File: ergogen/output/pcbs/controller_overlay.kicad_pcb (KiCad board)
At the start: 2 copper layers, 20 x 60.6 mm, 0 parts

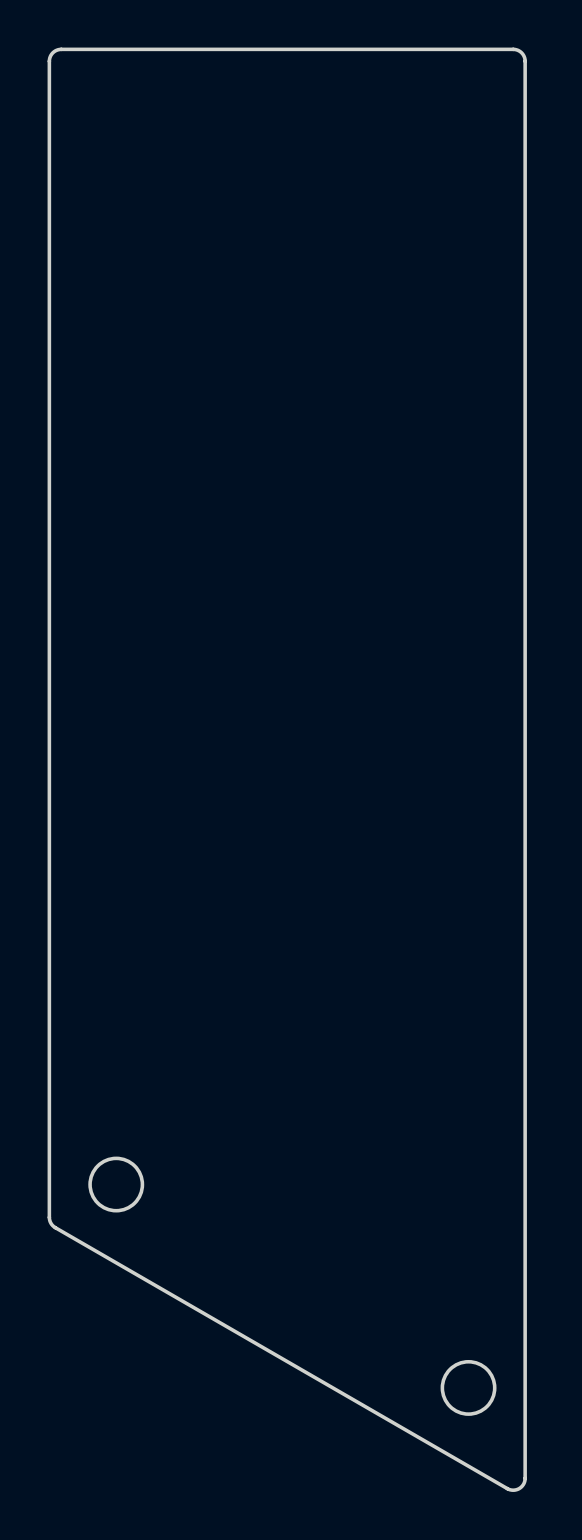
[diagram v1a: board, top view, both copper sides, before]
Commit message: Fix key positions to exactly match the corne
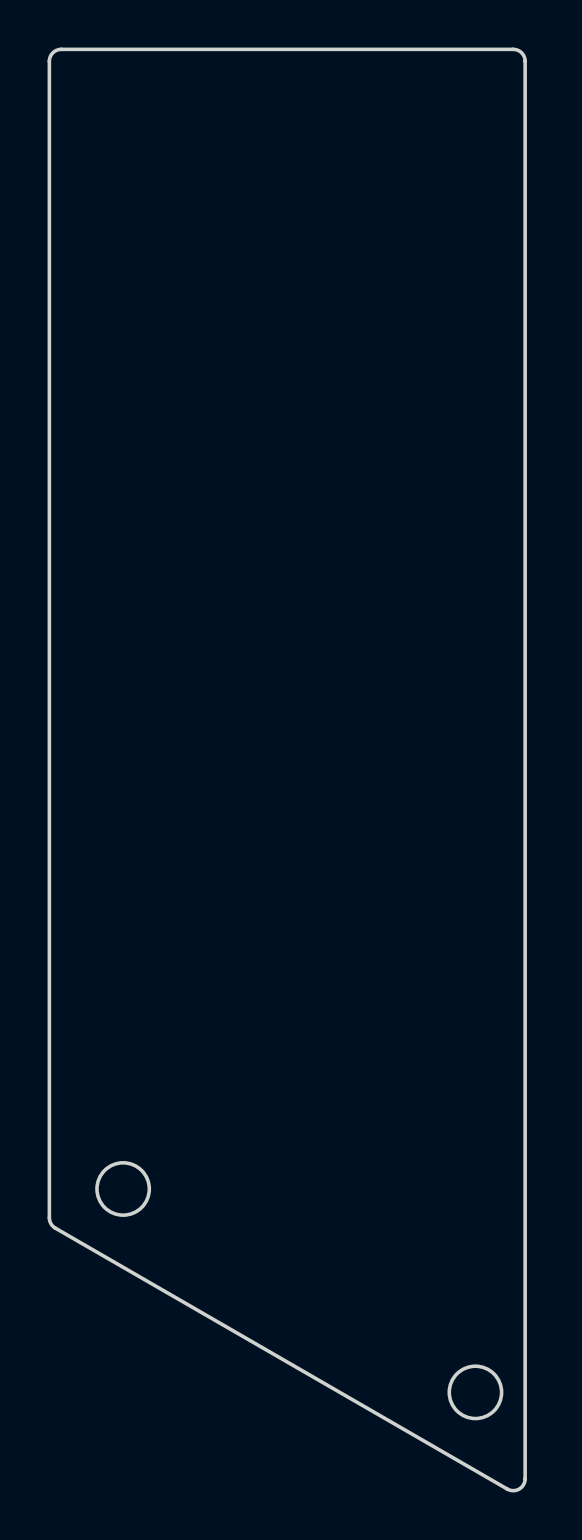
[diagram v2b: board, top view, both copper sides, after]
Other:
- outline, holes or cut-outs redrawn
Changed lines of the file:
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@@
     (add_net "")
   )
-            (gr_line (start 224.5 112.5673240447331) (end 224.5 53) (angle 90) (layer Edge.Cuts) (width 0.15))
+            (gr_line (start 224.5 112.58641018336651) (end 224.5 53) (angle 90) (layer Edge.Cuts) (width 0.15))
 (gr_line (start 224 52.5) (end 205 52.5) (angle 90) (layer Edge.Cuts) (width 0.15))
-(gr_line (start 204.5 53) (end 204.5 101.59766890124159) (angle 90) (layer Edge.Cuts) (width 0.15))
-(gr_line (start 223.74999999999997 113.00033674473308) (end 204.75 102.0306816012416) (angle 90) (layer Edge.Cuts) (width 0.15))
+(gr_line (start 204.5 53) (end 204.5 101.616755039875) (angle 90) (layer Edge.Cuts) (width 0.15))
+(gr_line (start 223.74999999999997 113.01942288336649) (end 204.75 102.04976773987501) (angle 90) (layer Edge.Cuts) (width 0.15))
 (gr_arc (start 224 53) (end 224.5 53) (angle -90) (layer Edge.Cuts) (width 0.15))
 (gr_arc (start 205 53) (end 205 52.5) (angle -90) (layer Edge.Cuts) (width 0.15))
-(gr_arc (start 205 101.59766890124159) (end 204.5 101.59766890124159) (angle -59.999999891584196) (layer Edge.Cuts) (width 0.15))
-(gr_arc (start 224 112.5673240447331) (end 223.75 113.0003367447331) (angle -120.0000001084203) (layer Edge.Cuts) (width 0.15))
-(gr_circle (center 207.31164829999997 100.2187534) (end 208.41164829999997 100.2187534) (layer Edge.Cuts) (width 0.15))
-(gr_circle (center 222.12068269999997 108.7687534) (end 223.22068269999997 108.7687534) (layer Edge.Cuts) (width 0.15))
+(gr_arc (start 205 101.616755039875) (end 204.5 101.616755039875) (angle -59.999999891584196) (layer Edge.Cuts) (width 0.15))
+(gr_arc (start 224 112.58641018336651) (end 223.75 113.01942288336652) (angle -120.0000001084203) (layer Edge.Cuts) (width 0.15))
+(gr_circle (center 207.6013921 100.4051232) (end 208.7013921 100.4051232) (layer Edge.Cuts) (width 0.15))
+(gr_circle (center 222.4104265 108.9551232) (end 223.5104265 108.9551232) (layer Edge.Cuts) (width 0.15))
 )

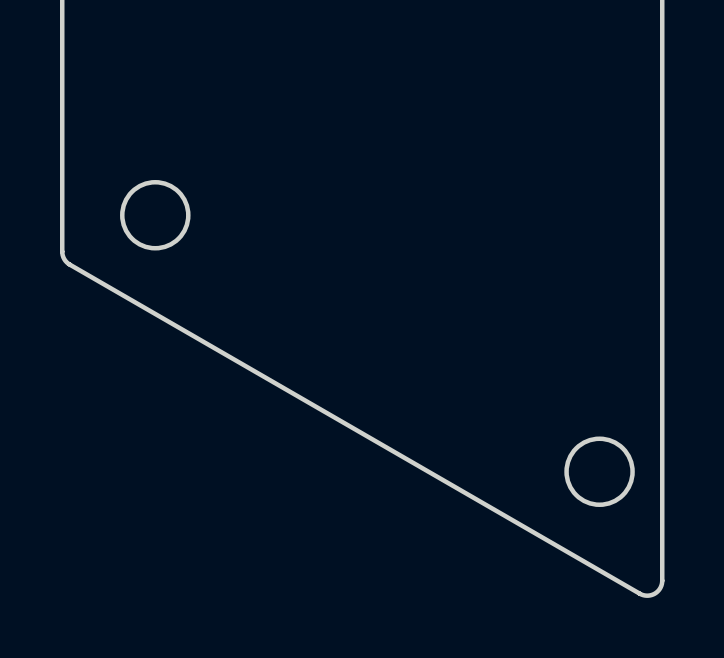
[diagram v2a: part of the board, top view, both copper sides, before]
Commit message: Fix MCU cover mounting holes position
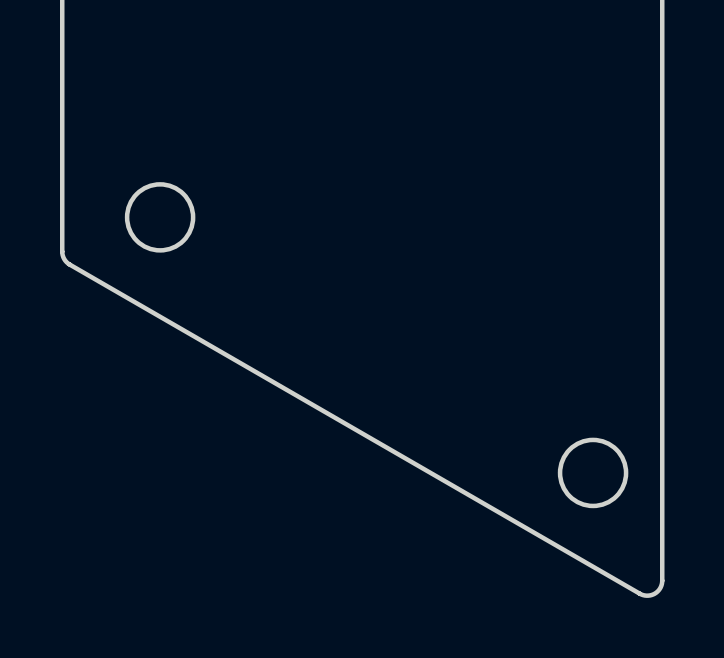
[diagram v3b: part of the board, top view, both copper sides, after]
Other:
- outline, holes or cut-outs redrawn
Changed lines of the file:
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@@
 (gr_arc (start 205 101.616755039875) (end 204.5 101.616755039875) (angle -59.999999891584196) (layer Edge.Cuts) (width 0.15))
 (gr_arc (start 224 112.58641018336651) (end 223.75 113.01942288336652) (angle -120.0000001084203) (layer Edge.Cuts) (width 0.15))
-(gr_circle (center 207.6013921 100.4051232) (end 208.7013921 100.4051232) (layer Edge.Cuts) (width 0.15))
-(gr_circle (center 222.4104265 108.9551232) (end 223.5104265 108.9551232) (layer Edge.Cuts) (width 0.15))
+(gr_circle (center 207.762 100.476) (end 208.862 100.476) (layer Edge.Cuts) (width 0.15))
+(gr_circle (center 222.194 108.995) (end 223.29399999999998 108.995) (layer Edge.Cuts) (width 0.15))
 )

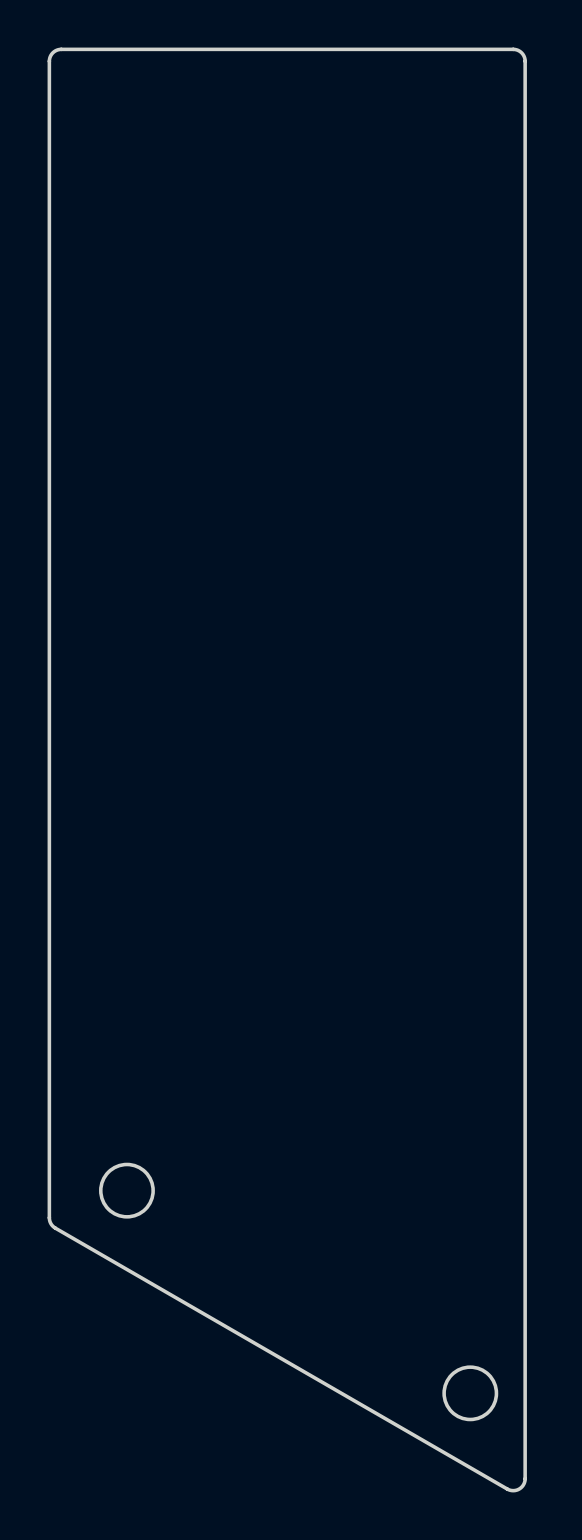
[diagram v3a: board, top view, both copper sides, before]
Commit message: Overhaul outlines making use of intersect
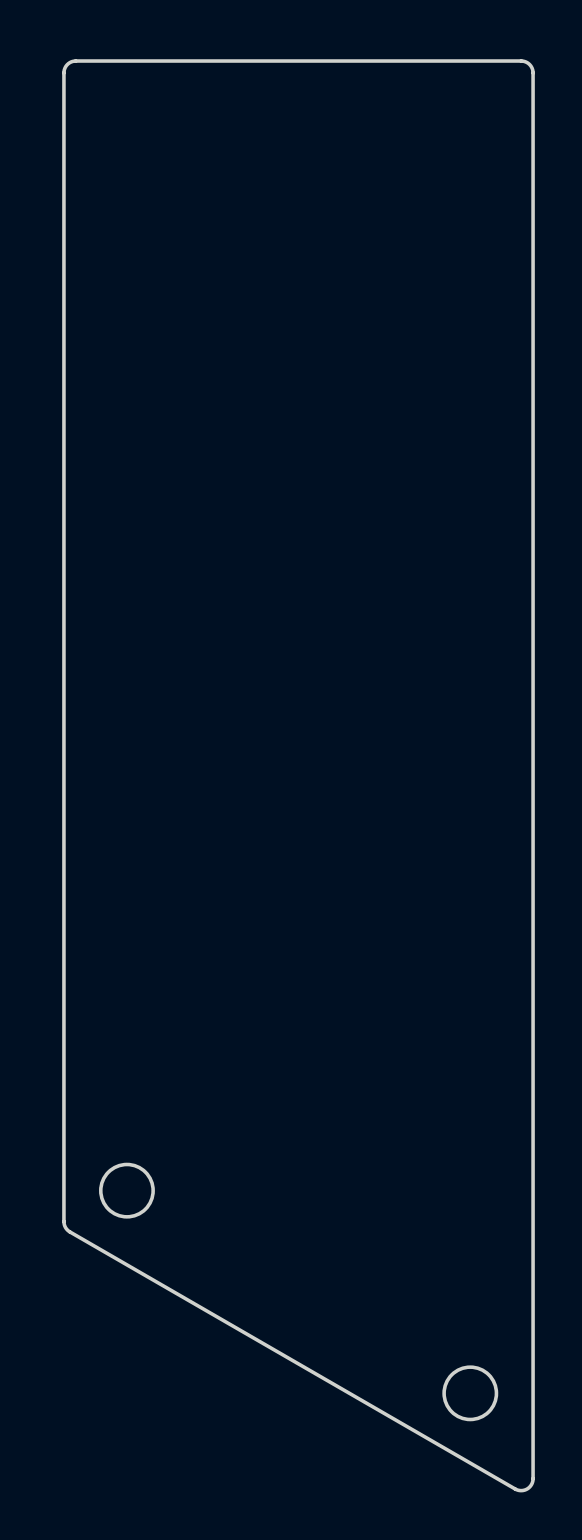
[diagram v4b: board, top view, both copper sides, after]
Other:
- board size 20 x 60.6 mm -> 19.7 x 60.1 mm
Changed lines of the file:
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@@
     (add_net "")
   )
-            (gr_line (start 224.5 112.58641018336651) (end 224.5 53) (angle 90) (layer Edge.Cuts) (width 0.15))
-(gr_line (start 224 52.5) (end 205 52.5) (angle 90) (layer Edge.Cuts) (width 0.15))
-(gr_line (start 204.5 53) (end 204.5 101.616755039875) (angle 90) (layer Edge.Cuts) (width 0.15))
-(gr_line (start 223.74999999999997 113.01942288336649) (end 204.75 102.04976773987501) (angle 90) (layer Edge.Cuts) (width 0.15))
-(gr_arc (start 224 53) (end 224.5 53) (angle -90) (layer Edge.Cuts) (width 0.15))
-(gr_arc (start 205 53) (end 205 52.5) (angle -90) (layer Edge.Cuts) (width 0.15))
-(gr_arc (start 205 101.616755039875) (end 204.5 101.616755039875) (angle -59.999999891584196) (layer Edge.Cuts) (width 0.15))
-(gr_arc (start 224 112.58641018336651) (end 223.75 113.01942288336652) (angle -120.0000001084203) (layer Edge.Cuts) (width 0.15))
+            (gr_line (start 205.113 101.77697755907997) (end 205.113 53.49) (angle 90) (layer Edge.Cuts) (width 0.15))
+(gr_line (start 205.613 52.99) (end 224.333 52.99) (angle 90) (layer Edge.Cuts) (width 0.15))
+(gr_line (start 224.833 53.49) (end 224.833 112.58497459811554) (angle 90) (layer Edge.Cuts) (width 0.15))
+(gr_line (start 224.08299999999997 113.01798729811554) (end 205.36299999999997 102.20999025907994) (angle 90) (layer Edge.Cuts) (width 0.15))
+(gr_arc (start 205.613 53.49) (end 205.613 52.99) (angle -90) (layer Edge.Cuts) (width 0.15))
+(gr_arc (start 224.333 53.49) (end 224.833 53.49) (angle -90) (layer Edge.Cuts) (width 0.15))
+(gr_arc (start 224.333 112.58497459811554) (end 224.083 113.01798729811554) (angle -120.00000010841867) (layer Edge.Cuts) (width 0.15))
+(gr_arc (start 205.613 101.77697755907997) (end 205.113 101.77697755907997) (angle -59.999999891579705) (layer Edge.Cuts) (width 0.15))
 (gr_circle (center 207.762 100.476) (end 208.862 100.476) (layer Edge.Cuts) (width 0.15))
 (gr_circle (center 222.194 108.995) (end 223.29399999999998 108.995) (layer Edge.Cuts) (width 0.15))

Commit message: Refresh generated files.
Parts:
- added H1: , Screw_Hole, F.Cu at (207.8, 100.5)
- added H2: , Screw_Hole, F.Cu at (222.2, 109.0)
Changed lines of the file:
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@@
     (add_net "")
+  )
+  (module "Screw_Hole" (layer F.Cu)
+      (at 207.762 100.476 0)
+      (fp_text reference "H1" (at 0 2.55) (layer F.SilkS) hide (effects (font (size 1 1) (thickness 0.15))))
+      (pad "" np_thru_hole circle (at 0 0) (size 2.2 2.2) (drill 2.2) (layers *.Cu *.Mask))
+  )
+  (module "Screw_Hole" (layer F.Cu)
+      (at 222.194 108.995 0)
+      (fp_text reference "H2" (at 0 2.55) (layer F.SilkS) hide (effects (font (size 1 1) (thickness 0.15))))
+      (pad "" np_thru_hole circle (at 0 0) (size 2.2 2.2) (drill 2.2) (layers *.Cu *.Mask))
   )
             (gr_line (start 205.113 101.77697755907997) (end 205.113 53.49) (angle 90) (layer Edge.Cuts) (width 0.15))

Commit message: Update TRRS footprint pinout and module
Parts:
- removed H1, H2: , Screw_Hole
- added MH1: , ceoloide:mounting_hole_npth, F.Cu at (207.8, 100.5)
- added MH2: , ceoloide:mounting_hole_npth, F.Cu at (222.2, 109.0)
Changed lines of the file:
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@@
   (title_block
     (title controller_overlay)
-    (rev 0.1)
+    (rev 0.2)
     (company ceoloide)
   )
@@
     (add_net "")
   )
-  (module "Screw_Hole" (layer F.Cu)
+  (module "ceoloide:mounting_hole_npth" (layer F.Cu)
       (at 207.762 100.476 0)
-      (fp_text reference "H1" (at 0 2.55) (layer F.SilkS) hide (effects (font (size 1 1) (thickness 0.15))))
-      (pad "" np_thru_hole circle (at 0 0) (size 2.2 2.2) (drill 2.2) (layers *.Cu *.Mask))
+      (fp_text reference "MH1" (at 0 2.55 0) (layer F.SilkS) hide (effects (font (size 1 1) (thickness 0.15))))
+      (pad "" np_thru_hole circle (at 0 0 0) (size 2.2 2.2) (drill 2.2) (layers *.Cu *.Mask))
   )
-  (module "Screw_Hole" (layer F.Cu)
+  (module "ceoloide:mounting_hole_npth" (layer F.Cu)
       (at 222.194 108.995 0)
-      (fp_text reference "H2" (at 0 2.55) (layer F.SilkS) hide (effects (font (size 1 1) (thickness 0.15))))
-      (pad "" np_thru_hole circle (at 0 0) (size 2.2 2.2) (drill 2.2) (layers *.Cu *.Mask))
+      (fp_text reference "MH2" (at 0 2.55 0) (layer F.SilkS) hide (effects (font (size 1 1) (thickness 0.15))))
+      (pad "" np_thru_hole circle (at 0 0 0) (size 2.2 2.2) (drill 2.2) (layers *.Cu *.Mask))
   )
             (gr_line (start 205.113 101.77697755907997) (end 205.113 53.49) (angle 90) (layer Edge.Cuts) (width 0.15))

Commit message: Update assets
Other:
- net class Default removed

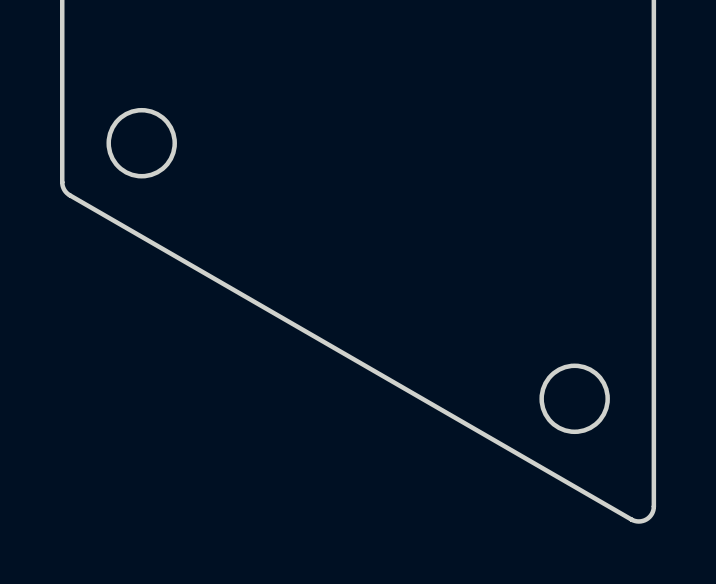
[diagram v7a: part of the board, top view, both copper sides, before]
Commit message: Switch to KiCad 8 PCB template and require Ergogen v4.1.0
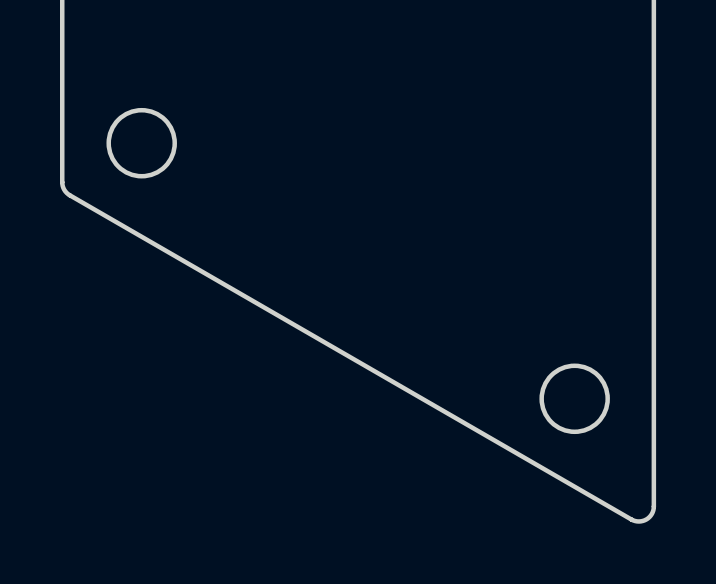
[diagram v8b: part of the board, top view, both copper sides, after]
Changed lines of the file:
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@@
 	(title_block
 		(title "controller_overlay")
+		(date "2024-04-11")
 		(rev "0.2")
 		(company "ceoloide")
@@
 			)
 		)
-		(attr through_hole)
 		(pad "" np_thru_hole circle
 			(at 0 0)
@@
 			)
 		)
-		(attr through_hole)
 		(pad "" np_thru_hole circle
 			(at 0 0)
@@
 		)
 	)
+	(gr_line
+		(start 224.083 113.017987)
+		(end 205.363 102.20999)
+		(stroke
+			(width 0.15)
+			(type default)
+		)
+		(layer "Edge.Cuts")
+	)
 	(gr_arc
 		(start 224.333 52.99)
@@
 		(stroke
 			(width 0.15)
-			(type solid)
+			(type default)
+		)
+		(layer "Edge.Cuts")
+	)
+	(gr_circle
+		(center 207.762 100.476)
+		(end 208.862 100.476)
+		(stroke
+			(width 0.15)
+			(type default)
+		)
+		(fill none)
+		(layer "Edge.Cuts")
+	)
+	(gr_arc
+		(start 224.833 112.584975)
+		(mid 224.582996 113.017974)
+		(end 224.083 113.017987)
+		(stroke
+			(width 0.15)
+			(type default)
+		)
+		(layer "Edge.Cuts")
+	)
+	(gr_arc
+		(start 205.363 102.20999)
+		(mid 205.179996 102.026976)
+		(end 205.113 101.776978)
+		(stroke
+			(width 0.15)
+			(type default)
 		)
 		(layer "Edge.Cuts")
@@
 		(stroke
 			(width 0.15)
-			(type solid)
+			(type default)
 		)
 		(layer "Edge.Cuts")
@@
 		(stroke
 			(width 0.15)
-			(type solid)
-		)
-		(layer "Edge.Cuts")
-	)
-	(gr_line
-		(start 224.083 113.017987)
-		(end 205.363 102.20999)
-		(stroke
-			(width 0.15)
-			(type solid)
-		)
-		(layer "Edge.Cuts")
-	)
-	(gr_arc
-		(start 205.363 102.209991)
-		(mid 205.179987 102.026978)
-		(end 205.113 101.776978)
-		(stroke
-			(width 0.15)
-			(type solid)
-		)
-		(layer "Edge.Cuts")
-	)
-	(gr_line
-		(start 224.833 53.49)
-		(end 224.833 112.584975)
-		(stroke
-			(width 0.15)
-			(type solid)
-		)
-		(layer "Edge.Cuts")
-	)
-	(gr_arc
-		(start 224.832999 112.584975)
-		(mid 224.582999 113.017987)
-		(end 224.083 113.017987)
-		(stroke
-			(width 0.15)
-			(type solid)
+			(type default)
 		)
 		(layer "Edge.Cuts")
@@
 		(stroke
 			(width 0.15)
-			(type solid)
+			(type default)
 		)
 		(fill none)
 		(layer "Edge.Cuts")
 	)
-	(gr_circle
-		(center 207.762 100.476)
-		(end 208.862 100.476)
-		(stroke
-			(width 0.15)
-			(type solid)
-		)
-		(fill none)
+	(gr_line
+		(start 224.833 53.49)
+		(end 224.833 112.584975)
+		(stroke
+			(width 0.15)
+			(type default)
+		)
 		(layer "Edge.Cuts")
 	)
@@
 		(stroke
 			(width 0.15)
-			(type solid)
-		)
-		(layer "Edge.Cuts")
+			(type default)
+		)
+		(layer "Edge.Cuts")
